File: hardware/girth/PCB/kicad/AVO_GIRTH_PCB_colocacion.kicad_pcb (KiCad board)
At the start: 4 copper layers, 65.5 x 43.5 mm, 115 parts, among them J1 USB-C 16P, J2 BATERÍA 1S, K1 G6KU-2F-Y DC3, Q1 AO3401A, Q10 AO3401A, Q11 AO3400A, Q12 2N7002, Q13 AO3400A, Q14 AO3401A, Q15 2N7002, Q16 2N7002, Q2 AO3401A, Q3 AO3401A, SW1 REED (1), SW2 REED (2), U1 BQ51013BRHLR, U2 BQ24072RGTR, U3 RT9080-33GJ5, U4 ESP32-C6-MINI-1U-N4, U5 BNO085, U6 USBLC6-2SC6, Y1 32,768 kHz 12,5 pF

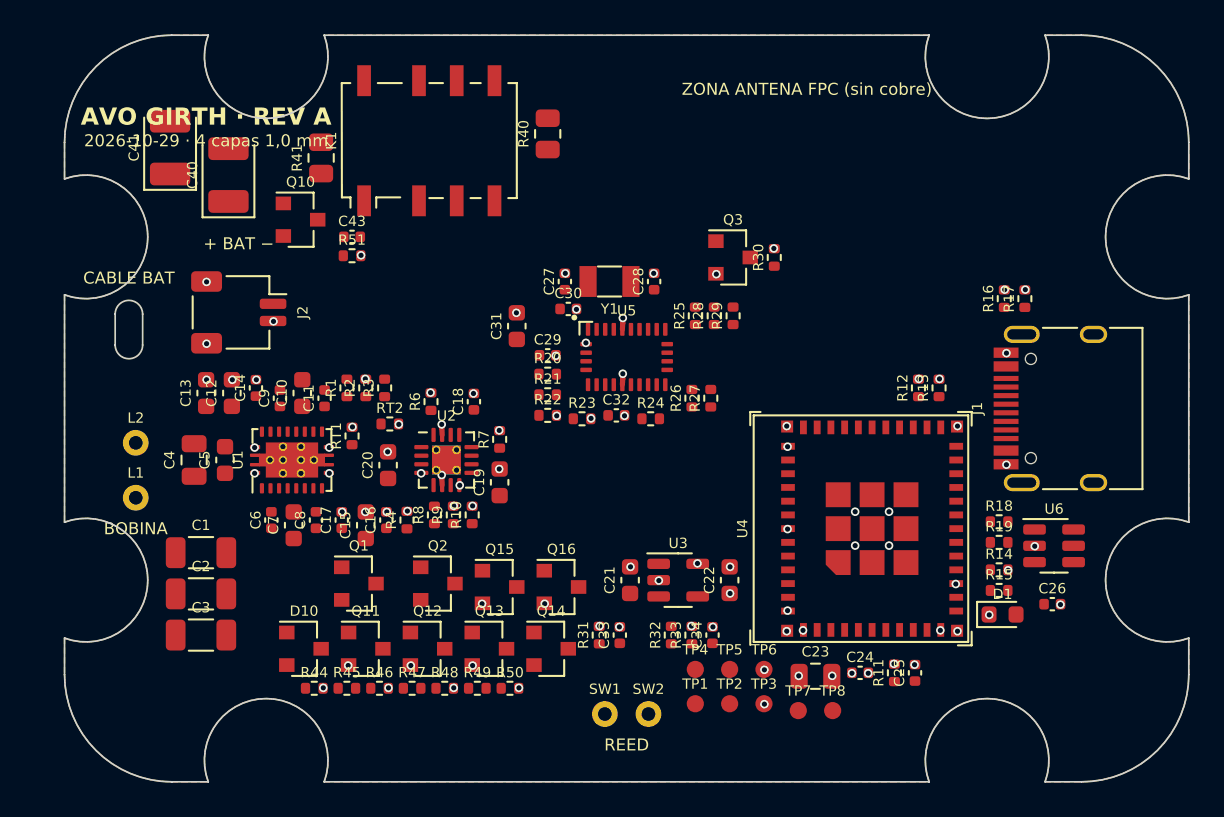
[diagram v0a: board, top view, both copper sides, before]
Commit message: PCB cincha: DSN sin los planos GND exteriores (se añaden tras el ruteado); límite de pasadas de Freerouting
Co-Authored-By: Claude Opus 5.5 <noreply@anthropic.com>
Claude-Session: https://claude.ai/code/session_01CHDvF8BfHwPLkrFs9S3ECm
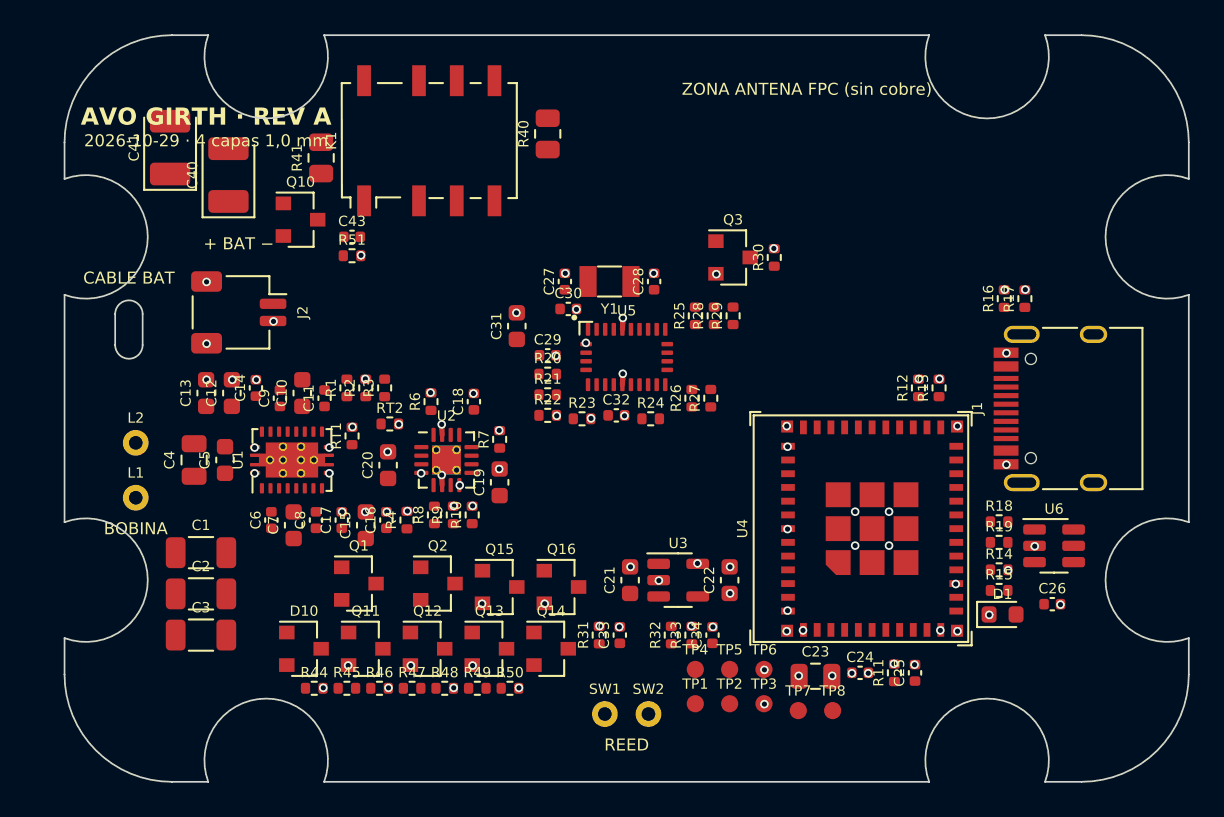
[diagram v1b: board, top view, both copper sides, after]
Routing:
- removed copper zone on B.Cu, net GND
- removed copper zone on F.Cu, net GND

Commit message: PCB cincha: más espacio alrededor del BQ51013B, bandas sin pistas en los arcos del borde, separación de taladros, serigrafía y avisos de DRC/ERC
Co-Authored-By: Claude Opus 5.5 <noreply@anthropic.com>
Claude-Session: https://claude.ai/code/session_01CHDvF8BfHwPLkrFs9S3ECm
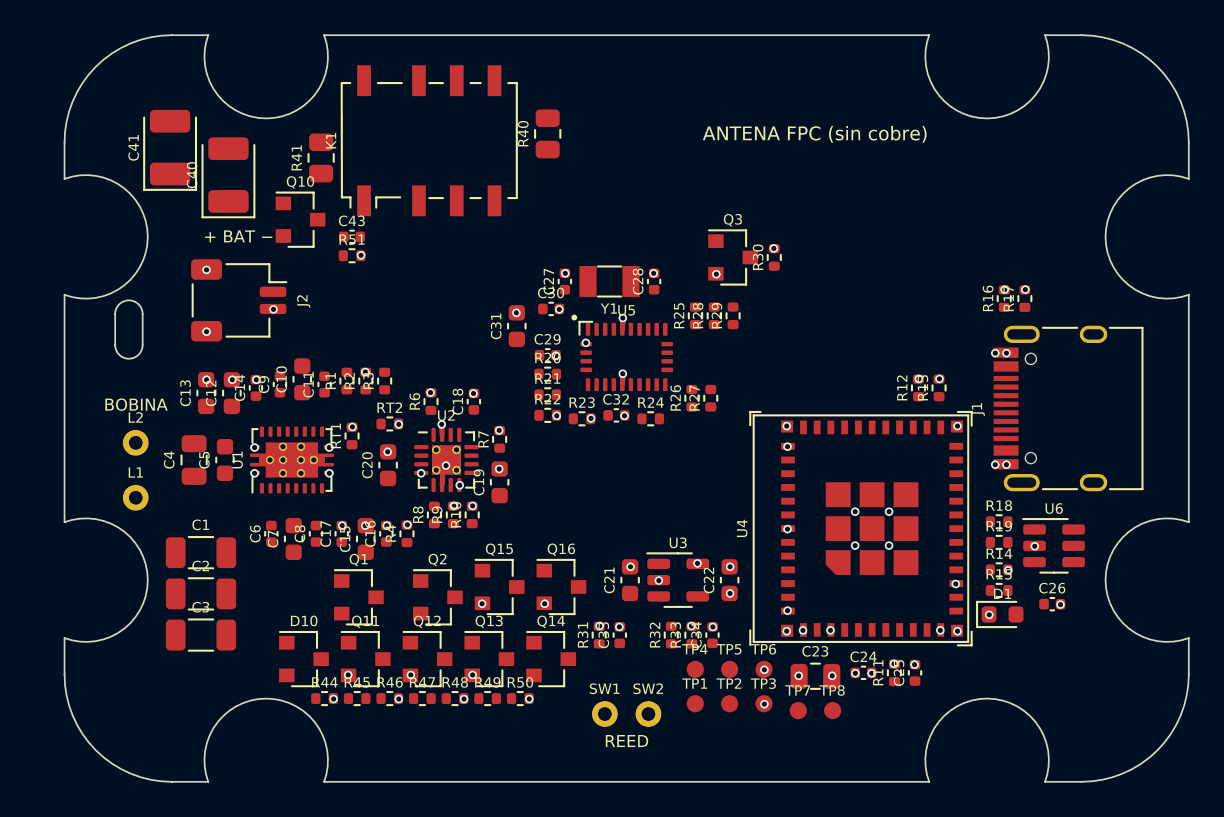
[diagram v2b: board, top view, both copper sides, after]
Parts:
- moved C30 1.00 mm to (95.6, 94.2)
- moved R44 0.85 mm to (82.4, 116.9)
- moved R46 0.85 mm to (86.2, 116.9)
- moved R49 0.85 mm to (91.9, 116.9)
- moved R45 0.85 mm to (84.3, 116.9)
- moved R47 0.85 mm to (88.1, 116.9)
- moved R48 0.85 mm to (90.0, 116.9)
- moved R50 0.85 mm to (93.8, 116.9)
- moved C11 0.80 mm to (82.4, 98.6)
- moved C9 0.80 mm to (79.8, 98.6)
- moved C10 0.80 mm to (81.1, 98.3)
- moved C15 0.80 mm to (84.8, 107.6)
- moved C16 0.80 mm to (86.0, 107.3)
- moved C17 0.80 mm to (83.4, 107.3)
- moved C6 0.80 mm to (79.3, 107.3)
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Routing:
- net GND: track 4.70 -> 6.53 mm, vias 78 -> 80
- net +3V3: track 0.42 -> 0.45 mm, vias 14 -> 15
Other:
- board text added: "4 capas 1,0 mm · ENIG"
- board text added: "ANTENA FPC (sin cobre)"
- board text added: "AVO GIRTH · REV A · 2026-10-29"
- board text removed: "2026-10-29 · 4 capas 1,0 mm"
- board text removed: "AVO GIRTH REV A"
- board text removed: "AVO GIRTH · REV A"
- board text removed: "CABLE BAT"
- board text removed: "ZONA ANTENA FPC (sin cobre)"

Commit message: PCB cincha: pre-ruteo de los condensadores del BQ51013B, USB y relé; condensadores sur girados hacia el chip
Co-Authored-By: Claude Opus 5.5 <noreply@anthropic.com>
Claude-Session: https://claude.ai/code/session_01CHDvF8BfHwPLkrFs9S3ECm
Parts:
- turned C15 to 270 degrees
- turned C16 to 270 degrees
- turned C17 to 270 degrees
- turned C6 to 270 degrees
- turned C7 to 270 degrees
- turned C8 to 270 degrees
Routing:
- net USB_DM_C: track 0.00 -> 17.1 mm, vias 0 -> 3
- net USB_DP_C: track 0.00 -> 14.9 mm
- net RLY_NO: track 0.00 -> 9.52 mm
- net USB_DM: track 0.00 -> 3.45 mm
- net USB_DP: track 0.00 -> 3.28 mm
- net QI_COMM2: track 0.00 -> 2.92 mm
- net QI_CLAMP2: track 0.00 -> 2.61 mm
- net QI_COMM1: track 0.00 -> 2.60 mm
- net QI_BOOT2: track 0.00 -> 2.27 mm
- net QI_CLAMP1: track 0.00 -> 2.26 mm
- net QI_BOOT1: track 0.00 -> 2.17 mm

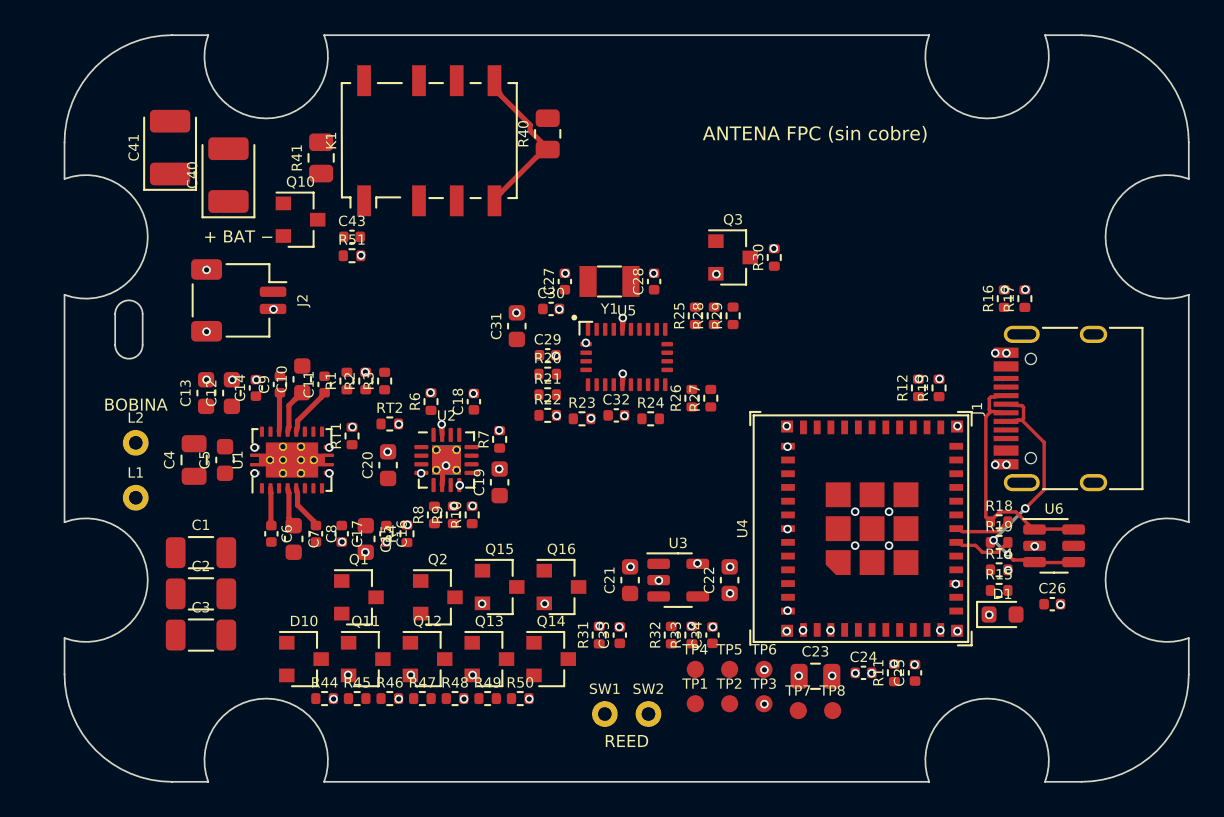
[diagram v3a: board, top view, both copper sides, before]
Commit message: PCB cincha: pre-ruteo de la zona Qi/cargador/USB antes de Freerouting
Co-Authored-By: Claude Opus 5.5 <noreply@anthropic.com>
Claude-Session: https://claude.ai/code/session_01CHDvF8BfHwPLkrFs9S3ECm
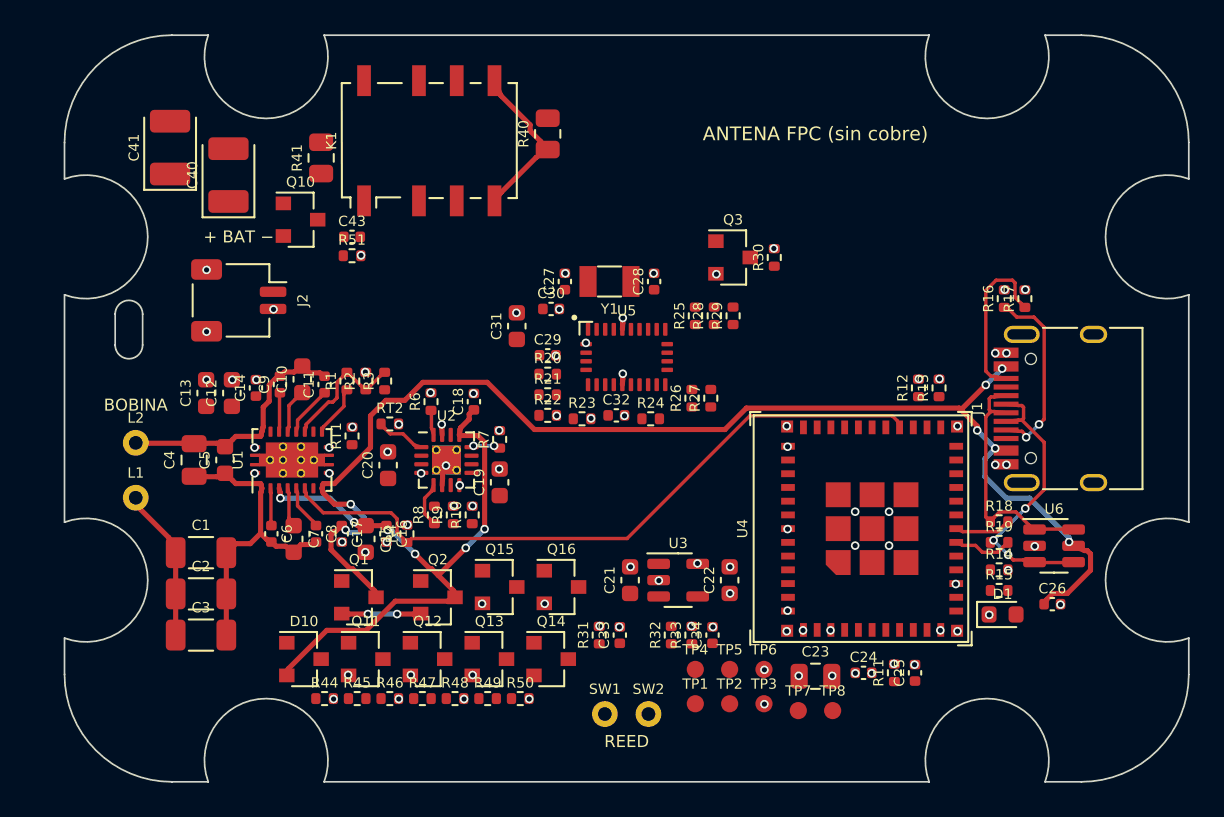
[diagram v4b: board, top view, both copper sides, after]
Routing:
- net VBUS: track 0.00 -> 76.3 mm, vias 0 -> 7
- net QI_CHG: track 0.00 -> 40.1 mm
- net VIN5: track 0.00 -> 37.5 mm, vias 0 -> 6
- net QI_AC1: track 0.00 -> 18.2 mm
- net QI_AC2: track 0.00 -> 14.6 mm
- net CC1: track 0.00 -> 11.0 mm, vias 0 -> 2
- net CC2: track 0.00 -> 9.70 mm
- net QI_COIL1: track 0.00 -> 8.82 mm
- net QI_FOD: track 0.00 -> 7.60 mm
- net AD_SRC: track 0.00 -> 4.60 mm, vias 0 -> 2
- net QI_ILIM: track 0.00 -> 3.00 mm
- net CHG_TS: track 0.00 -> 2.89 mm
- net CHG_EN2: track 0.00 -> 2.67 mm
- net CHG_ILIM: track 0.00 -> 1.69 mm, vias 0 -> 2
- net CHG_ISET: track 0.00 -> 1.45 mm

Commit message: PCB cincha: zona del cargador más holgada y pre-ruteo reducido
Co-Authored-By: Claude Opus 5.5 <noreply@anthropic.com>
Claude-Session: https://claude.ai/code/session_01CHDvF8BfHwPLkrFs9S3ECm
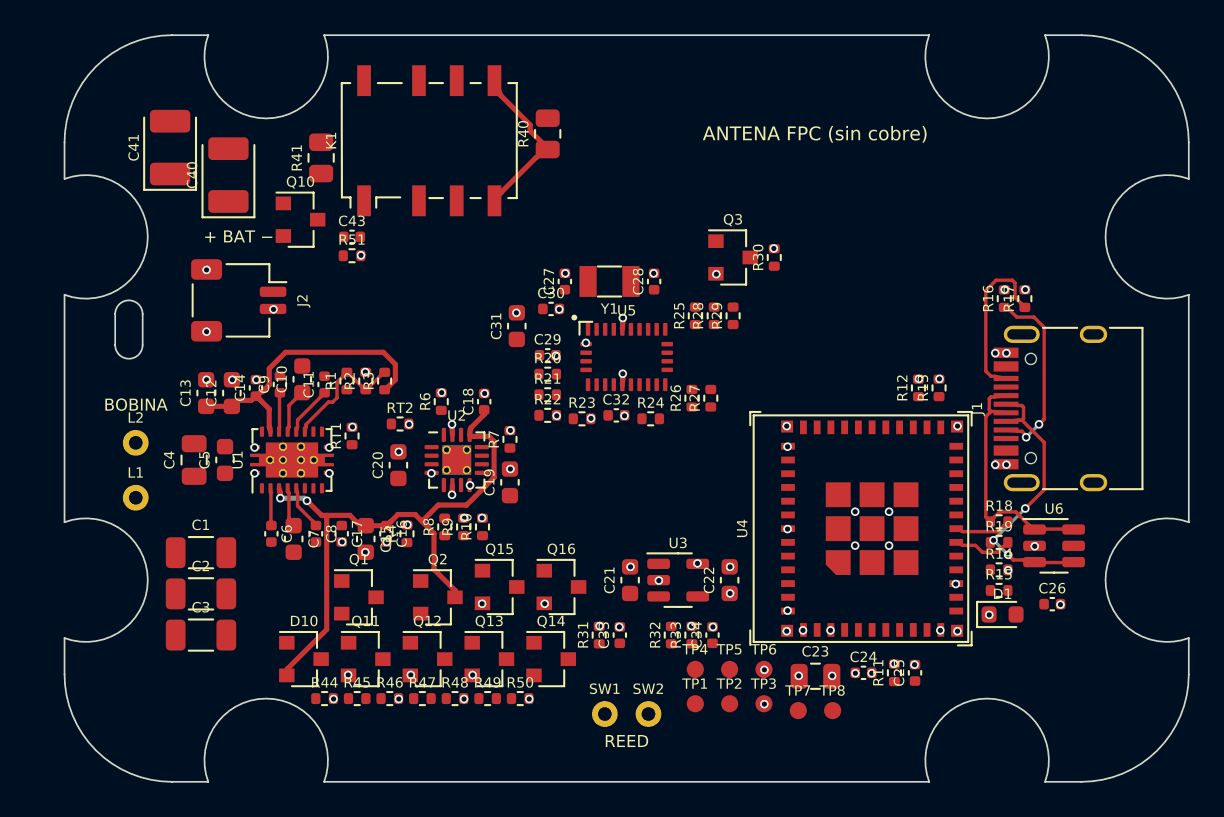
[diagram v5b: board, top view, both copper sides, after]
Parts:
- moved R8 0.92 mm to (89.4, 106.9)
- moved R10 0.92 mm to (91.6, 106.9)
- moved R9 0.92 mm to (90.5, 106.9)
- moved C18 0.60 mm to (91.7, 99.6)
- moved C19 0.60 mm to (93.2, 104.3)
- moved C20 0.60 mm to (86.7, 103.3)
- moved R6 0.60 mm to (89.2, 99.6)
- moved R7 0.60 mm to (93.2, 101.8)
- moved RT2 0.60 mm to (86.8, 100.9)
- moved U2 0.60 mm to (90.1, 103.0)
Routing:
- net VBUS: track 76.3 -> 0.00 mm, vias 7 -> 0
- net QI_CHG: track 40.1 -> 0.00 mm
- net QI_AC1: track 18.2 -> 0.00 mm
- net QI_RECT: track 0.00 -> 17.3 mm
- net QI_AC2: track 14.6 -> 0.00 mm
- net QI_COIL1: track 8.82 -> 0.00 mm
- net AD_SRC: track 4.60 -> 0.00 mm, vias 2 -> 0
- net QI_ILIM: track 3.00 -> 0.00 mm
- net CHG_TS: track 2.89 -> 0.00 mm
- net CHG_EN2: track 2.67 -> 0.00 mm
- net CHG_ILIM: track 1.69 -> 0.00 mm, vias 2 -> 0
- net CHG_ISET: track 1.45 -> 0.00 mm
- net VIN5: track 37.5 -> 36.1 mm, vias 6 -> 2
- net GND: track 6.53 -> 5.87 mm

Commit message: PCB cincha: pre-ruteo también de las redes del BQ24072
Co-Authored-By: Claude Opus 5.5 <noreply@anthropic.com>
Claude-Session: https://claude.ai/code/session_01CHDvF8BfHwPLkrFs9S3ECm
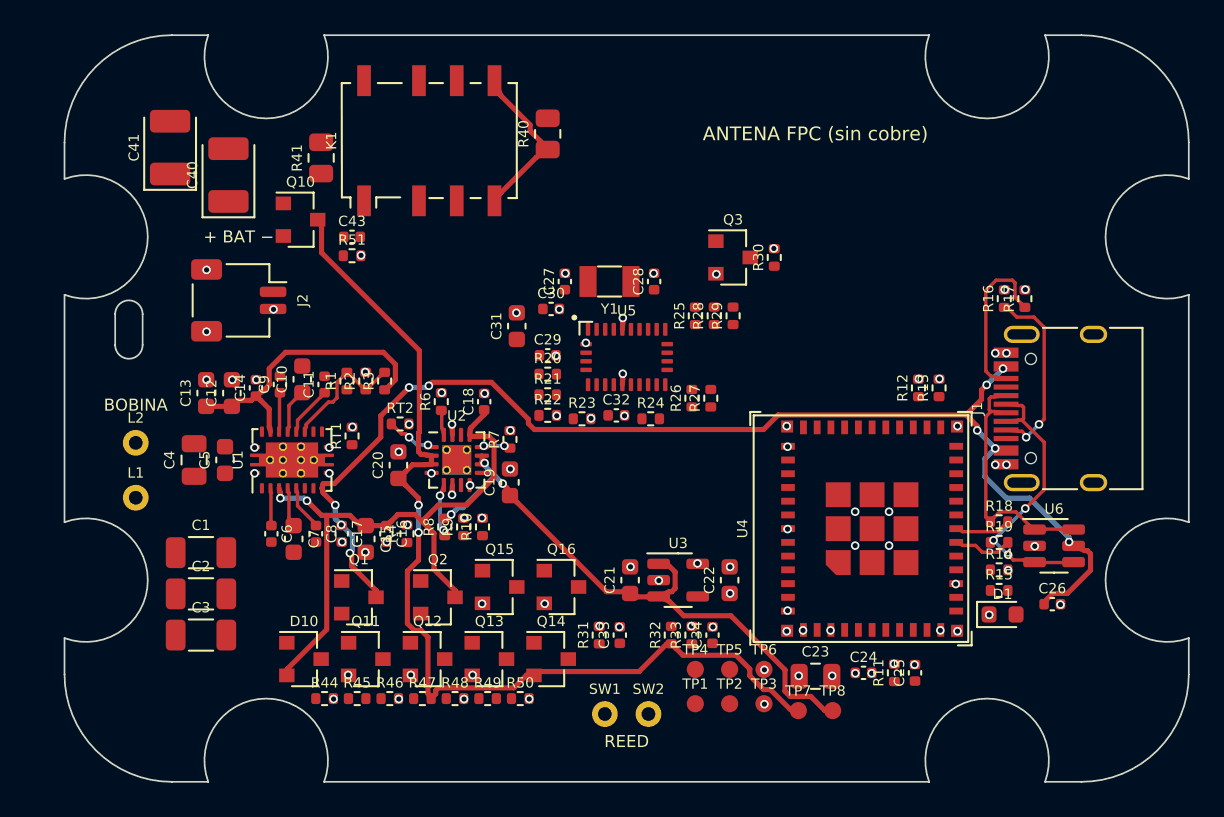
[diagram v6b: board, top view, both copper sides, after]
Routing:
- net VBUS: track 0.00 -> 72.7 mm, vias 0 -> 10
- net VBAT: track 0.00 -> 58.6 mm, vias 0 -> 2
- net VSYS: track 0.00 -> 34.8 mm, vias 0 -> 3
- net CHG_EN2: track 0.00 -> 3.10 mm, vias 0 -> 2
- net CHG_TS: track 0.00 -> 2.89 mm, vias 0 -> 2
- net CHG_ILIM: track 0.00 -> 1.69 mm, vias 0 -> 2
- net CHG_ISET: track 0.00 -> 1.45 mm
